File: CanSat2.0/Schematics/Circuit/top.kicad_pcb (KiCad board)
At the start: 2 copper layers, 62.2 x 63 mm, 28 parts, among them J1 Conn_01x09, K1 SI7021, Q1 BSS138, Q2 BSS138, U1 LSM303AGRTR, U2 VEML6070, U3 TSL2591, U4 microservo, U6 MPL3115A2

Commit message: PCBs
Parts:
- J1, R6: moved to B.Cu
- moved R3 62.7 mm to (58.6, 79.0)
- moved R2 59.6 mm to (57.6, 74.1)
- moved J1 50.3 mm to (46.0, 70.0), turned to 300 degrees
- moved C11 49.7 mm to (39.1, 30.0)
- moved C1 48.5 mm to (41.2, 79.2)
- moved R6 46.4 mm to (47.5, 64.4)
- moved C5 45.9 mm to (39.1, 27.0), turned to 270 degrees
- moved R7 43.0 mm to (44.5, 62.6), turned to 180 degrees
- moved C7 42.7 mm to (45.7, 57.6), turned to 180 degrees
- moved C2 42.5 mm to (45.7, 56.2), turned to 180 degrees
- moved Q2 42.4 mm to (45.7, 60.2)
- moved Q1 41.9 mm to (42.1, 60.3), turned to 270 degrees
- moved R5 40.1 mm to (43.0, 57.6)
- moved C9 38.5 mm to (39.0, 31.9), turned to 180 degrees
- moved C10 37.9 mm to (39.0, 33.3), turned to 180 degrees
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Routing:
- net +3V3: track 0.00 -> 171.1 mm, vias 0 -> 6
- net /SDA: track 0.00 -> 163.4 mm, vias 0 -> 6
- net /SCL: track 0.00 -> 158.2 mm, vias 0 -> 6
- net GND: track 0.00 -> 127.3 mm, vias 0 -> 8
- net /SER_P: track 0.00 -> 40.9 mm, vias 0 -> 3
- net /TX_GPS: track 0.00 -> 30.0 mm, vias 0 -> 5
- net /LED: track 0.00 -> 22.6 mm, vias 0 -> 1
- net Net-(C10-Pad2): track 0.00 -> 13.8 mm
- net +5V: track 0.00 -> 11.1 mm, vias 0 -> 1
- net Net-(C10-Pad1): track 0.00 -> 9.01 mm, vias 0 -> 2
- net /RX_GPS: track 0.00 -> 8.20 mm, vias 0 -> 1
- net /RX_GPSL: track 0.00 -> 3.79 mm
- net /TX_GPSL: track 0.00 -> 3.72 mm
- net Net-(R2-Pad1): track 0.00 -> 3.71 mm
- net Net-(R3-Pad2): track 0.00 -> 2.37 mm
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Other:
- board size 62.2 x 63 mm -> 64 x 64 mm

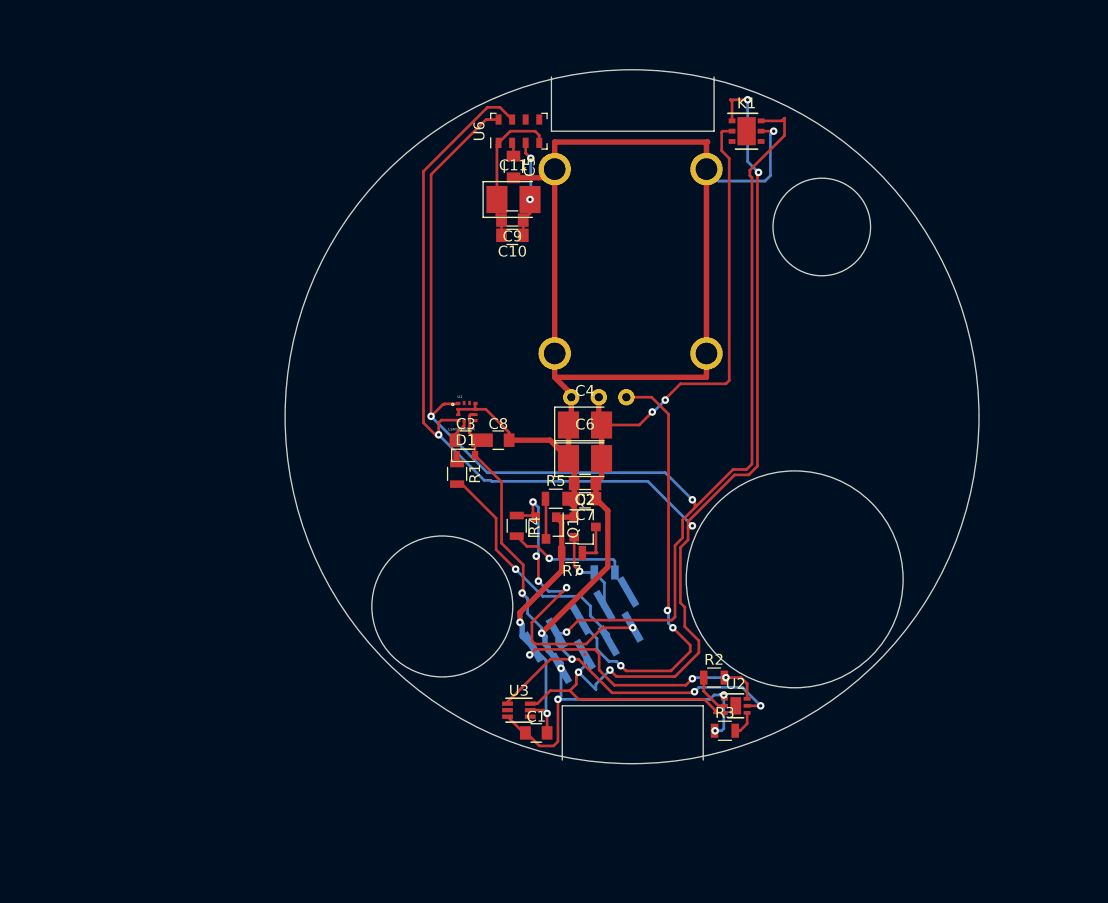
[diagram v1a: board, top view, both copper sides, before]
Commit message: Add three top boards and some other circuitry and modelling
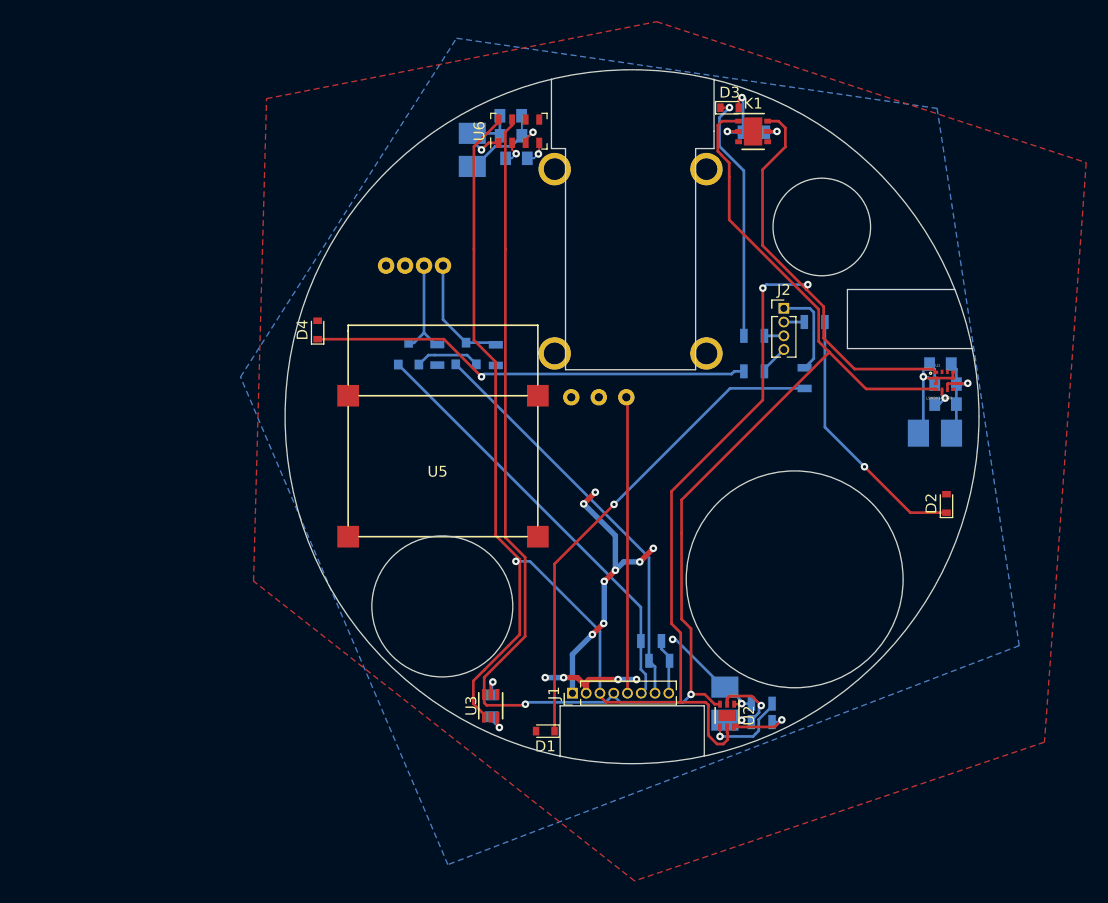
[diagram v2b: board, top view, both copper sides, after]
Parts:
- added D2: LED, Diodes_SMD:D_0603, F.Cu at (79.0, 58.0)
- added D3: LED, Diodes_SMD:D_0603, F.Cu at (59.0, 21.5)
- added D4: LED, Diodes_SMD:D_0603, F.Cu at (21.0, 42.0)
- added J2: Conn_01x04, Pin_Headers:Pin_Header_Straight_1x04_Pitch1.27mm, F.Cu at (64.0, 40.0)
- added R10: 105, Resistors_SMD:R_0805, B.Cu at (61.3, 45.8)
- added R8: 105, Resistors_SMD:R_0805, B.Cu at (66.8, 41.3)
- added R9: 105, Resistors_SMD:R_0805, B.Cu at (61.3, 42.5)
- added U5: GPS, CanSat:GPS, F.Cu at (32.6, 48.1)
- C1, C10, C11, C2, C3, C4, C5, C6, C7, C8, C9, Q1, Q2, R2, R3, R4, R5, R7: moved to B.Cu
- J1: value Conn_01x09 -> Conn_01x08; footprint Pin_Headers:Pin_Header_Straight_1x09_Pitch1.27mm_SMD_Pin1Left -> Pin_Headers:Pin_Header_Straight_1x08_Pitch1.27mm; moved to F.Cu
- R1: value 150 -> 105; moved to B.Cu
- moved C1 49.6 mm to (78.9, 47.0), turned to 180 degrees
- moved C3 44.4 mm to (78.9, 48.8)
- moved U1 44.2 mm to (78.8, 46.7)
- moved C8 36.9 mm to (61.2, 23.8)
- moved C7 35.1 mm to (78.4, 45.1)
- moved R1 33.2 mm to (65.9, 46.4), turned to 90 degrees
- moved C6 32.4 mm to (77.9, 51.5)
- moved C4 28.8 mm to (58.6, 76.5), turned to 90 degrees
- moved D1 26.5 mm to (42.0, 79.0), turned to 180 degrees
- moved Q2 22.8 mm to (29.4, 44.2), turned to 90 degrees
- moved C2 22.2 mm to (37.1, 76.7), turned to 90 degrees
- moved R7 22.1 mm to (32.0, 44.3), turned to 270 degrees
- moved R4 18.1 mm to (52.5, 72.5), turned to 0 degrees
- moved Q1 17.7 mm to (34.7, 44.2), turned to 90 degrees
- moved R5 14.4 mm to (37.4, 44.3), turned to 270 degrees
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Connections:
- C10 pad 1: Net-(C10-Pad1) -> GND
- C10 pad 2: Net-(C10-Pad2) -> +3V3
- C11 pad 1: Net-(C10-Pad2) -> +3V3
- C11 pad 2: Net-(C10-Pad1) -> GND
- C9 pad 1: Net-(C10-Pad1) -> GND
- C9 pad 2: Net-(C10-Pad2) -> +3V3
- J1 pad 6: /LED -> /RX_GPS
- J1 pad 7: /RX_GPS -> /TX_GPS
- J1 pad 8: /TX_GPS -> +5V
- R1 pad 2: /LED -> /LED1
- U6 pad 1: Net-(C10-Pad2) -> +3V3
- U6 pad 3: Net-(C10-Pad1) -> GND
- U6 pad 4: Net-(C10-Pad2) -> +3V3
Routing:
- net +3V3: track 171.1 -> 70.8 mm, vias 6 -> 15
- net GND: track 127.3 -> 50.7 mm, vias 8 -> 11
- net Net-(D1-Pad1): track 0.00 -> 45.2 mm, vias 0 -> 1
- net Net-(D4-Pad1): track 0.00 -> 41.0 mm, vias 0 -> 1
- net /RX_GPS: track 8.20 -> 40.3 mm, vias 1 -> 0
- net Net-(D2-Pad1): track 0.00 -> 24.2 mm, vias 0 -> 1
- net Net-(D3-Pad1): track 0.00 -> 23.2 mm, vias 0 -> 1
- net /LED: track 22.6 -> 0.00 mm, vias 1 -> 0
- net /SCL: track 158.2 -> 176.7 mm, vias 6 -> 3
- net Net-(C10-Pad2): track 13.8 -> 0.00 mm
- net /SER_P: track 40.9 -> 27.3 mm, vias 3 -> 0
- net Net-(C10-Pad1): track 9.01 -> 0.00 mm, vias 2 -> 0
- net /TX_GPS: track 30.0 -> 38.5 mm, vias 5 -> 0
- net /LED1: track 0.00 -> 8.39 mm
- net /TX_GPSL: track 3.72 -> 10.8 mm
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- added copper zone on B.Cu, net +3V3
- added copper zone on F.Cu, net GND
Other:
- outline, holes or cut-outs redrawn
- net class Default: clearance 0.203 -> 0.17; trace_width 0.25 -> 0.17
- rule trace_clearance: 0.203 -> 0.17
- rule trace_min: 0.203 -> 0.165

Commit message: Add new pcbs - center and bottom - and fill the lower half of the model
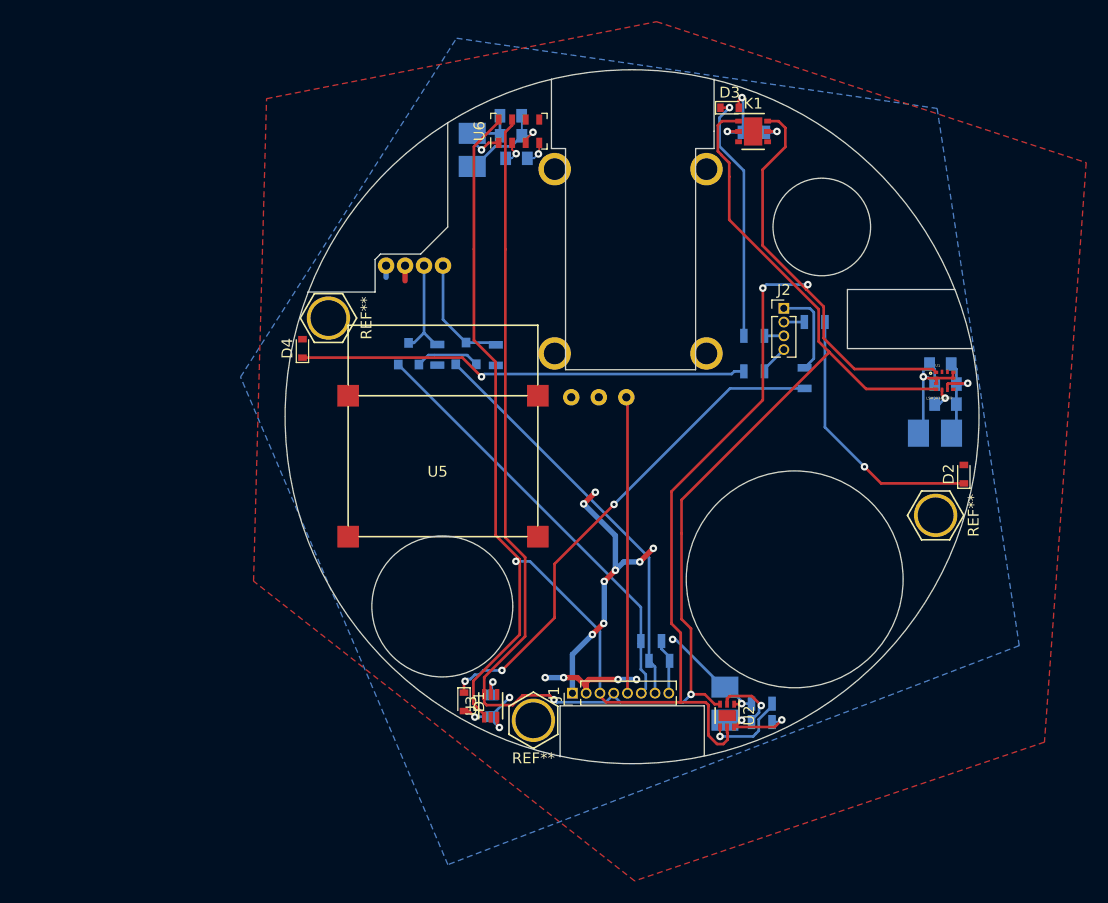
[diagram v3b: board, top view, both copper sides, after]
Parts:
- added REF**: Standoff, CanSat:Standoff, F.Cu at (40.9, 78.0)
- added REF**: Standoff, CanSat:Standoff, F.Cu at (78.0, 59.1)
- added REF**: Standoff, CanSat:Standoff, F.Cu at (22.0, 40.9)
- moved D1 7.97 mm to (34.5, 76.3), turned to 270 degrees
- moved D2 3.14 mm to (80.6, 55.3)
- moved D4 2.20 mm to (19.6, 43.7)
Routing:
- net GND: track 50.7 -> 57.8 mm, vias 11 -> 13
- net Net-(D1-Pad1): track 45.2 -> 46.5 mm, vias 1 -> 3
- net +3V3: track 70.8 -> 71.8 mm
- net Net-(D4-Pad1): track 41.0 -> 41.7 mm
- net /SDA: track 156.3 -> 156.8 mm
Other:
- outline, holes or cut-outs redrawn

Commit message: Edit final version of pcbs, gerbers generated
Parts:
- added C12: 10 uF, Capacitors_Tantalum_SMD:CP_Tantalum_Case-T_EIA-3528-12_Reflow, B.Cu at (44.3, 73.4)
- moved R7 5.34 mm to (26.7, 44.0)
- moved R5 5.24 mm to (32.2, 44.2)
- moved D1 0.34 mm to (34.8, 76.3)
- moved Q1 0.26 mm to (34.5, 44.4), turned to 0 degrees
- moved Q2 0.14 mm to (29.5, 44.1), turned to 0 degrees
- moved R2 0.14 mm to (62.0, 78.0)
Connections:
- Q1 pad 2: /TX_GPS -> /TX_GPSL
- Q1 pad 3: /TX_GPSL -> /TX_GPS
- Q2 pad 2: /RX_GPS -> /RX_GPSL
- Q2 pad 3: /RX_GPSL -> /RX_GPS
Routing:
- net GND: track 57.8 -> 128.6 mm, vias 13 -> 23
- net +3V3: track 71.8 -> 84.4 mm
- net /SCL: track 176.7 -> 179.3 mm, vias 3 -> 5
- net /TX_GPSL: track 10.8 -> 8.73 mm
- net /SDA: track 156.8 -> 156.2 mm, vias 2 -> 4
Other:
- outline, holes or cut-outs redrawn
- net class Default: clearance 0.17 -> 0.165
- rule trace_clearance: 0.17 -> 0.165
